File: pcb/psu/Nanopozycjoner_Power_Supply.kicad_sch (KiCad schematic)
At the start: 0 parts

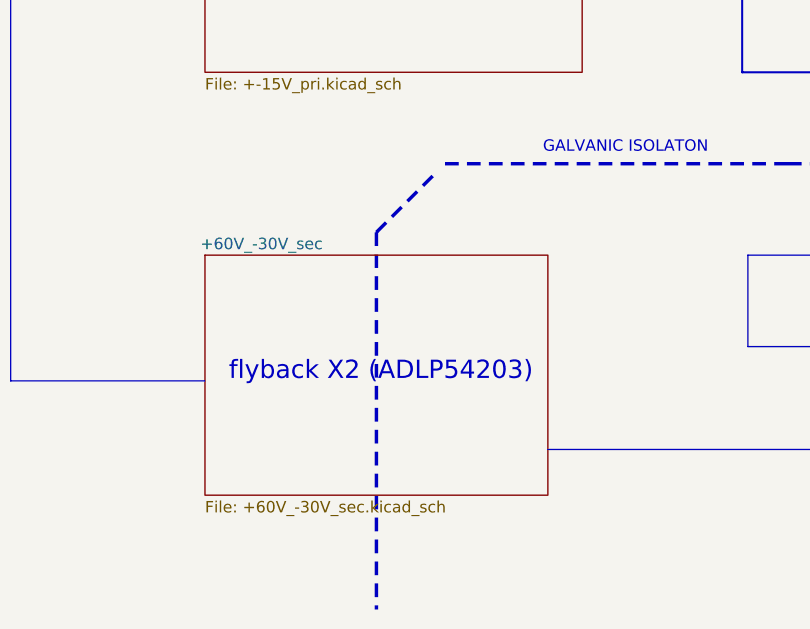
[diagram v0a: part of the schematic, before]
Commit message: poprawki do schematu psu
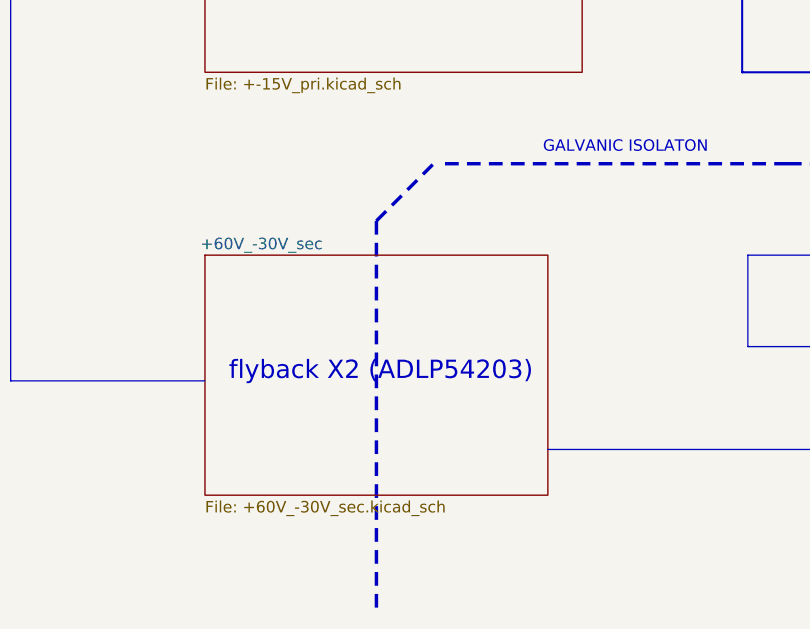
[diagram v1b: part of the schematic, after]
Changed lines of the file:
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@@
 	(polyline
 		(pts
-			(xy 128.27 121.92) (xy 134.62 115.57)
+			(xy 128.27 120.65) (xy 134.62 114.3)
 		)
 		(stroke
@@
 	(polyline
 		(pts
-			(xy 128.27 121.92) (xy 128.27 163.83)
+			(xy 128.27 120.65) (xy 128.27 163.83)
 		)
 		(stroke
@@
 		)
 	)
-	(label ""
-		(at 129.54 120.65 0)
-		(effects
-			(font
-				(size 1.27 1.27)
-			)
-			(justify left bottom)
-		)
-	)

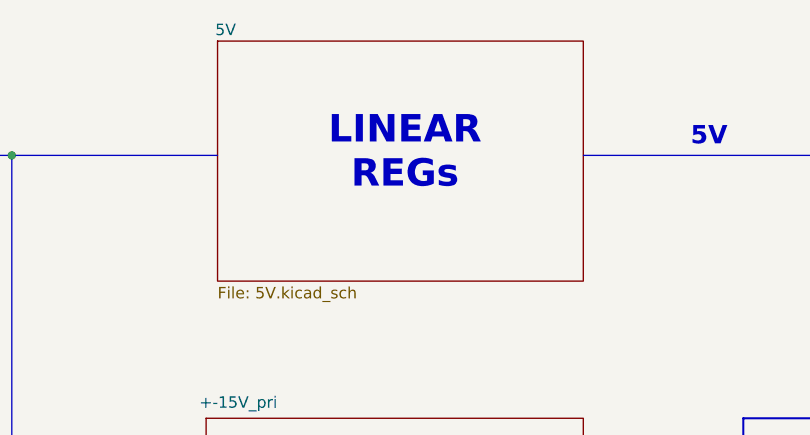
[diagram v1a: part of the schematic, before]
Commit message: added PSU PCB design files
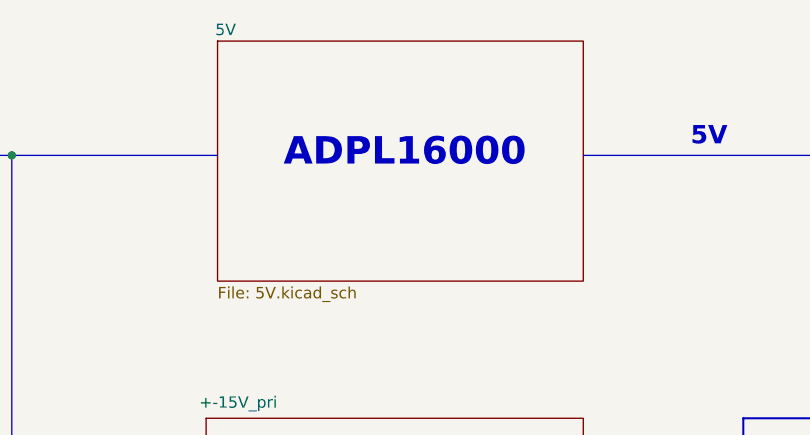
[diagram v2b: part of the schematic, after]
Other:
- note added: "ADPL16000"
- note removed: "LINEAR REGs"
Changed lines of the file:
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@@
 		)
 	)
-	(text "LINEAR\nREGs"
+	(text "ADPL16000\n"
 		(exclude_from_sim no)
 		(at 131.318 48.006 0)
